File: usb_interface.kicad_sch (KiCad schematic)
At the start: 56 parts, among them J7 GCT USB4105-GF-A-120, J8 PD_I2C DEBUG, Q1 CSD25480F3, Q2 CSD15380F3, Q3 CSD25480F3, Q4 CSD15380F3, U3 TVS2200DRV, U4 TPD8S300/A, U5 TI TPS25751DREFR, U6 CAT24C256

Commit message: oops add this
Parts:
- removed C35: 10uF, Capacitor_SMD:C_1206_3216Metric, symbol Device:C_Small
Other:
- note added: "7 x 10uF"
- note removed: "8 x 10uF"
- moved on the sheet: C26, C27, C29, C30, C32, C34

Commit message: assign lcsc part numbers
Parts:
- C26, C29, C30, C32, C34: LCSC Part C14860 -> C33546013
- C27, C28: LCSC Part C49326770 -> C33546013
- R35, R38: LCSC Part C2902636 -> C54951138
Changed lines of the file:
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@@
 			)
 		)
-		(property "LCSC Part" "C14860"
+		(property "LCSC Part" "C33546013"
 			(at 114.3 66.04 0)
 			(hide yes)
@@
 			)
 		)
-		(property "LCSC Part" "C14860"
+		(property "LCSC Part" "C33546013"
 			(at 118.11 66.04 0)
 			(hide yes)
@@
 			)
 		)
-		(property "LCSC Part" "C49326770"
+		(property "LCSC Part" "C33546013"
 			(at 110.49 66.04 0)
 			(hide yes)
@@
 			)
 		)
-		(property "LCSC Part" "C2902636"
+		(property "LCSC Part" "C54951138"
 			(at 232.41 74.93 0)
 			(hide yes)
@@
 			)
 		)
-		(property "LCSC Part" "C49326770"
+		(property "LCSC Part" "C33546013"
 			(at 106.68 66.04 0)
 			(hide yes)
@@
 			)
 		)
-		(property "LCSC Part" "C14860"
+		(property "LCSC Part" "C33546013"
 			(at 102.87 66.04 0)
 			(hide yes)
@@
 			)
 		)
-		(property "LCSC Part" "C2902636"
+		(property "LCSC Part" "C54951138"
 			(at 181.61 60.96 0)
 			(hide yes)
@@
 			)
 		)
-		(property "LCSC Part" "C14860"
+		(property "LCSC Part" "C33546013"
 			(at 125.73 66.04 0)
 			(hide yes)
@@
 			)
 		)
-		(property "LCSC Part" "C14860"
+		(property "LCSC Part" "C33546013"
 			(at 121.92 66.04 0)
 			(hide yes)

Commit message: new part numbers for out of stock components
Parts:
- Q1, Q3: LCSC Part C2869359 -> C2872850
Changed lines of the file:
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@@
 			)
 		)
-		(property "LCSC Part" "C2869359"
+		(property "LCSC Part" "C2872850"
 			(at 68.58 146.05 0)
 			(hide yes)
@@
 			)
 		)
-		(property "LCSC Part" "C2869359"
+		(property "LCSC Part" "C2872850"
 			(at 45.72 146.05 0)
 			(hide yes)

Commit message: backup before switching to kicad-nightly
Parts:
- J7: value GCT USB4105-GF-A-120 -> GCT USB4105-GF-A-060
- Q1, Q3: value CSD25480F3 -> CSD25481F4
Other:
- moved on the sheet: Q1, Q3
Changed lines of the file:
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@@
 	(wire
 		(pts
-			(xy 48.26 151.13) (xy 48.26 153.67)
+			(xy 48.26 152.4) (xy 48.26 153.67)
 		)
 		(stroke
@@
 	(wire
 		(pts
+			(xy 71.12 142.24) (xy 71.12 140.97)
+		)
+		(stroke
+			(width 0)
+			(type default)
+		)
+	)
+	(wire
+		(pts
 			(xy 181.61 114.3) (xy 181.61 116.84)
 		)
@@
 	(wire
 		(pts
+			(xy 48.26 142.24) (xy 48.26 140.97)
+		)
+		(stroke
+			(width 0)
+			(type default)
+		)
+	)
+	(wire
+		(pts
 			(xy 35.56 27.94) (xy 38.1 27.94)
 		)
@@
 	(wire
 		(pts
-			(xy 71.12 151.13) (xy 71.12 153.67)
+			(xy 71.12 152.4) (xy 71.12 153.67)
 		)
 		(stroke
@@
 	)
 	(label "GPIO2"
-		(at 63.5 146.05 180)
+		(at 63.5 147.32 180)
 		(effects
 			(font
@@
 	)
 	(label "GPIO2"
-		(at 40.64 146.05 180)
+		(at 40.64 147.32 180)
 		(effects
 			(font
@@
 	(symbol
 		(lib_id "Transistor_FET:CSD25480F3")
-		(at 68.58 146.05 0)
+		(at 68.58 147.32 0)
 		(mirror x)
 		(unit 1)
@@
 		(dnp no)
 		(property "Reference" "Q3"
-			(at 65.532 142.494 0)
+			(at 65.532 143.764 0)
 			(show_name no)
 			(do_not_autoplace no)
@@
 			)
 		)
-		(property "Value" "CSD25480F3"
-			(at 71.882 149.352 0)
+		(property "Value" "CSD25481F4"
+			(at 71.882 150.622 0)
 			(show_name no)
 			(do_not_autoplace no)
@@
 		)
 		(property "Footprint" "Package_DFN_QFN:Texas_PicoStar_DFN-3_0.69x0.60mm"
-			(at 98.933 141.351 0)
+			(at 98.933 142.621 0)
 			(hide yes)
 			(show_name no)
@@
 		)
 		(property "Datasheet" "https://www.ti.com/lit/ds/symlink/csd25480f3.pdf"
-			(at 99.695 143.637 0)
+			(at 99.695 144.907 0)
 			(hide yes)
 			(show_name no)
@@
 		)
 		(property "Description" "-1.7A Id, -20V Vds, P-Channel MOSFET, 159mOhm Ron,max @ 4.5Vgs, 0.70nC Qg,typ @ 4.5Vgs, PicoStar 0.73x0.64mm max, 0.69x0.60mm nom"
-			(at 68.58 146.05 0)
+			(at 68.58 147.32 0)
 			(hide yes)
 			(show_name no)
@@
 		)
 		(property "LCSC Part" "C2872850"
-			(at 68.58 146.05 0)
+			(at 68.58 147.32 0)
 			(hide yes)
 			(show_name no)
@@
 		)
 		(property "Voltage Rating" ""
-			(at 68.58 146.05 0)
+			(at 68.58 147.32 0)
 			(hide yes)
 			(show_name no)
@@
 		)
 		(property "Tolerance" ""
-			(at 68.58 146.05 0)
+			(at 68.58 147.32 0)
 			(hide yes)
 			(show_name no)
@@
 		)
 		(property "Capacitor Rating" ""
-			(at 68.58 146.05 0)
+			(at 68.58 147.32 0)
 			(hide yes)
 			(show_name no)
@@
 			)
 		)
-		(property "Value" "GCT USB4105-GF-A-120"
+		(property "Value" "GCT USB4105-GF-A-060"
 			(at 77.47 68.58 0)
 			(show_name no)
@@
 			)
 		)
+		(property "Capacitor Rating" ""
+			(at 77.47 88.9 0)
+			(hide yes)
+			(show_name no)
+			(do_not_autoplace no)
+			(effects
+				(font
+					(size 1.27 1.27)
+				)
+			)
+		)
 		(pin "B6"
 		)
@@
 	(symbol
 		(lib_id "Transistor_FET:CSD25480F3")
-		(at 45.72 146.05 0)
+		(at 45.72 147.32 0)
 		(mirror x)
 		(unit 1)
@@
 		(dnp no)
 		(property "Reference" "Q1"
-			(at 42.418 142.494 0)
+			(at 42.418 143.764 0)
 			(show_name no)
 			(do_not_autoplace no)
@@
 			)
 		)
-		(property "Value" "CSD25480F3"
-			(at 49.53 149.352 0)
+		(property "Value" "CSD25481F4"
+			(at 49.53 150.622 0)
 			(show_name no)
 			(do_not_autoplace no)
@@
 		)
 		(property "Footprint" "Package_DFN_QFN:Texas_PicoStar_DFN-3_0.69x0.60mm"
-			(at 76.073 141.351 0)
+			(at 76.073 142.621 0)
 			(hide yes)
 			(show_name no)
@@
 		)
 		(property "Datasheet" "https://www.ti.com/lit/ds/symlink/csd25480f3.pdf"
-			(at 76.835 143.637 0)
+			(at 76.835 144.907 0)
 			(hide yes)
 			(show_name no)
@@
 		)
 		(property "Description" "-1.7A Id, -20V Vds, P-Channel MOSFET, 159mOhm Ron,max @ 4.5Vgs, 0.70nC Qg,typ @ 4.5Vgs, PicoStar 0.73x0.64mm max, 0.69x0.60mm nom"
-			(at 45.72 146.05 0)
+			(at 45.72 147.32 0)
 			(hide yes)
 			(show_name no)
@@
 		)
 		(property "LCSC Part" "C2872850"
-			(at 45.72 146.05 0)
+			(at 45.72 147.32 0)
 			(hide yes)
 			(show_name no)
@@
 		)
 		(property "Voltage Rating" ""
-			(at 45.72 146.05 0)
+			(at 45.72 147.32 0)
 			(hide yes)
 			(show_name no)
@@
 		)
 		(property "Tolerance" ""
-			(at 45.72 146.05 0)
+			(at 45.72 147.32 0)
 			(hide yes)
 			(show_name no)
@@
 		)
 		(property "Capacitor Rating" ""
-			(at 45.72 146.05 0)
+			(at 45.72 147.32 0)
 			(hide yes)
 			(show_name no)

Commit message: lots of fixes!
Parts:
- removed U6: CAT24C256, Package_DFN_QFN:DFN-8-1EP_2x3mm_P0.5mm_EP0.61x2.2mm, symbol Memory_EEPROM:CAT24C256
- added U21: M24512-DFMC6TG, Package_DFN_QFN:DFN-8-1EP_3x2mm_P0.5mm_EP1.36x1.46mm, symbol easyeda2kicad:M24512-DFMC6TG
- C33, C36: LCSC Part C190579 -> C53426851
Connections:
- net GND: now also U21.4 (GND), U21.9 (EP)
- net I2C_PMIC_SCL: now also U21.6 (SCL)
- net I2C_PMIC_SDA: now also U21.5 (SDA)
- net PD_LDO_3V3: now also U21.8 (VCC)
- net WC: now also U21.7 (WC)
- net at RN1.5 (R4.2): now also U21.3 (E2)
- net at RN1.6 (R3.2): now also U21.2 (E1)
- net at RN1.7 (R2.2): now also U21.1 (E0)
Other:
- note added: "EEPROM 512Kb"
- note removed: "EEPROM 256Kb"
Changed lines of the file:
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@@
 (kicad_sch
-	(version 20260306)
+	(version 20260830)
 	(generator "eeschema")
-	(generator_version "10.0")
+	(generator_version "10.99")
 	(paper "A4")
 	(title_block
@@
 		)
 	)
-	(text "EEPROM 256Kb"
+	(text "EEPROM 512Kb"
 		(exclude_from_sim no)
 		(at 267.716 81.534 0)
@@
 	)
 	(junction
+		(at 241.3 104.14)
+		(diameter 0)
+		(color 0 0 0 0)
+	)
+	(junction
 		(at 71.12 140.97)
 		(diameter 0)
@@
 	(wire
 		(pts
+			(xy 241.3 104.14) (xy 243.84 104.14)
+		)
+		(stroke
+			(width 0)
+			(type default)
+		)
+	)
+	(wire
+		(pts
 			(xy 243.84 105.41) (xy 243.84 104.14)
 		)
@@
 	(wire
 		(pts
+			(xy 241.3 100.33) (xy 241.3 104.14)
+		)
+		(stroke
+			(width 0)
+			(type default)
+		)
+	)
+	(wire
+		(pts
 			(xy 118.11 63.5) (xy 118.11 62.23)
 		)
@@
 	(wire
 		(pts
-			(xy 229.87 104.14) (xy 243.84 104.14)
+			(xy 229.87 104.14) (xy 241.3 104.14)
 		)
 		(stroke
@@
 	)
 	(symbol
-		(lib_id "Memory_EEPROM:CAT24C256")
-		(at 243.84 90.17 0)
-		(unit 1)
-		(body_style 1)
-		(exclude_from_sim no)
-		(in_bom yes)
-		(on_board yes)
-		(in_pos_files yes)
-		(dnp no)
-		(property "Reference" "U6"
-			(at 234.442 81.026 0)
-			(show_name no)
-			(do_not_autoplace no)
-			(effects
-				(font
-					(size 1.27 1.27)
-				)
-				(justify left)
-			)
-		)
-		(property "Value" "CAT24C256"
-			(at 245.364 99.822 0)
-			(show_name no)
-			(do_not_autoplace no)
-			(effects
-				(font
-					(size 1.27 1.27)
-				)
-				(justify left)
-			)
-		)
-		(property "Footprint" "Package_DFN_QFN:DFN-8-1EP_2x3mm_P0.5mm_EP0.61x2.2mm"
-			(at 243.84 90.17 0)
-			(hide yes)
-			(show_name no)
-			(do_not_autoplace no)
-			(effects
-				(font
-					(size 1.27 1.27)
-				)
-			)
-		)
-		(property "Datasheet" "https://www.onsemi.cn/PowerSolutions/document/CAT24C256-D.PDF"
-			(at 241.808 108.204 0)
-			(hide yes)
-			(show_name no)
-			(do_not_autoplace no)
-			(effects
-				(font
-					(size 1.27 1.27)
-				)
-			)
-		)
-		(property "Description" "256 kb CMOS Serial EEPROM, DIP-8/SOIC-8/TSSOP-8/DFN-8"
-			(at 241.808 108.204 0)
-			(hide yes)
-			(show_name no)
-			(do_not_autoplace no)
-			(effects
-				(font
-					(size 1.27 1.27)
-				)
-			)
-		)
-		(property "LCSC Part" "C233771"
-			(at 243.84 90.17 0)
-			(hide yes)
-			(show_name no)
-			(do_not_autoplace no)
-			(effects
-				(font
-					(size 1.27 1.27)
-				)
-			)
-		)
-		(property "Voltage Rating" ""
-			(at 243.84 90.17 0)
-			(hide yes)
-			(show_name no)
-			(do_not_autoplace no)
-			(effects
-				(font
-					(size 1.27 1.27)
-				)
-			)
-		)
-		(property "Tolerance" ""
-			(at 243.84 90.17 0)
-			(hide yes)
-			(show_name no)
-			(do_not_autoplace no)
-			(effects
-				(font
-					(size 1.27 1.27)
-				)
-			)
-		)
-		(property "Capacitor Rating" ""
-			(at 243.84 90.17 0)
-			(hide yes)
-			(show_name no)
-			(do_not_autoplace no)
-			(effects
-				(font
-					(size 1.27 1.27)
-				)
-			)
-		)
-		(pin "7"
-		)
-		(pin "6"
-		)
-		(pin "5"
-		)
-		(pin "4"
-		)
-		(pin "3"
-		)
-		(pin "2"
-		)
-		(pin "1"
-		)
-		(pin "8"
-		)
-		(instances
-			(project "parsnip"
-				(path "/a9f1fdad-fb49-4185-a4ff-ad8f47273e4d"
-					(reference "U6")
-					(unit 1)
-				)
-			)
-		)
-	)
-	(symbol
 		(lib_id "Device:C_Small")
 		(at 54.61 88.9 0)
@@
 		(dnp no)
 		(property "Reference" "R36"
-			(at 183.642 55.88 0)
+			(at 184.15 53.848 0)
 			(show_name no)
 			(do_not_autoplace no)
@@
 		)
 		(property "Value" "2.2k"
-			(at 183.388 64.516 0)
+			(at 183.642 55.88 0)
 			(show_name no)
 			(do_not_autoplace no)
@@
 			)
 		)
-		(property "LCSC Part" "C190579"
+		(property "LCSC Part" "C53426851"
 			(at 129.54 85.09 0)
 			(hide yes)
@@
 			)
 		)
+		(property "MPN" ""
+			(at 129.54 85.09 0)
+			(hide yes)
+			(show_name no)
+			(do_not_autoplace no)
+			(effects
+				(font
+					(size 1.27 1.27)
+				)
+			)
+		)
 		(pin "1"
 		)
@@
 	)
 	(symbol
+		(lib_id "easyeda2kicad:M24512-DFMC6TG")
+		(at 242.57 86.36 0)
+		(unit 1)
+		(body_style 1)
+		(exclude_from_sim no)
+		(in_bom yes)
+		(on_board yes)
+		(in_pos_files yes)
+		(dnp no)
+		(property "Reference" "U21"
+			(at 236.474 81.28 0)
+			(show_name no)
+			(do_not_autoplace no)
+			(effects
+				(font
+					(size 1.27 1.27)
+				)
+			)
+		)
+		(property "Value" "M24512-DFMC6TG"
+			(at 254.254 99.822 0)
+			(show_name no)
+			(do_not_autoplace no)
+			(effects
+				(font
+					(size 1.27 1.27)
+				)
+			)
+		)
+		(property "Footprint" "Package_DFN_QFN:DFN-8-1EP_3x2mm_P0.5mm_EP1.36x1.46mm"
+			(at 243.84 109.728 0)
+			(hide yes)
+			(show_name no)
+			(do_not_autoplace no)
+			(effects
+				(font
+					(size 1.27 1.27)
+				)
+			)
+		)
+		(property "Datasheet" "https://lcsc.com/product-detail/Others_STMicroelectronics_M24512-DFMC6TG_STMicroelectronics-M24512-DFMC6TG_C222237.html"
+			(at 243.84 112.268 0)
+			(hide yes)
+			(show_name no)
+			(do_not_autoplace no)
+			(effects
+				(font
+					(size 1.27 1.27)
+				)
+			)
+		)
+		(property "Description" ""
+			(at 242.57 86.36 0)
+			(hide yes)
+			(show_name no)
+			(do_not_autoplace no)
+			(effects
+				(font
+					(size 1.27 1.27)
+				)
+			)
+		)
+		(property "Manufacturer" "ST(意法半导体)"
+			(at 243.84 114.808 0)
+			(hide yes)
+			(show_name no)
+			(do_not_autoplace no)
+			(effects
+				(font
+					(size 1.27 1.27)
+				)
+			)
+		)
+		(property "MPN" "M24512-DFMC6TG"
+			(at 243.84 117.348 0)
+			(hide yes)
+			(show_name no)
+			(do_not_autoplace no)
+			(effects
+				(font
+					(size 1.27 1.27)
+				)
+			)
+		)
+		(property "LCSC Part" "C222237"
+			(at 243.84 119.888 0)
+			(hide yes)
+			(show_name no)
+			(do_not_autoplace no)
+			(effects
+				(font
+					(size 1.27 1.27)
+				)
+			)
+		)
+		(property "Voltage Rating" ""
+			(at 242.57 86.36 0)
+			(hide yes)
+			(show_name no)
+			(do_not_autoplace no)
+			(effects
+				(font
+					(size 1.27 1.27)
+				)
+			)
+		)
+		(property "Tolerance" ""
+			(at 242.57 86.36 0)
+			(hide yes)
+			(show_name no)
+			(do_not_autoplace no)
+			(effects
+				(font
+					(size 1.27 1.27)
+				)
+			)
+		)
+		(pin "1"
+		)
+		(pin "2"
+		)
+		(pin "3"
+		)
+		(pin "4"
+		)
+		(pin "5"
+		)
+		(pin "6"
+		)
+		(pin "7"
+		)
+		(pin "8"
+		)
+		(pin "9"
+		)
+		(instances
+			(project "parsnip"
+				(path "/a9f1fdad-fb49-4185-a4ff-ad8f47273e4d"
+					(reference "U21")
+					(unit 1)
+				)
+			)
+		)
+	)
+	(symbol
 		(lib_id "Device:C_Small")
 		(at 102.87 66.04 0)
@@
 			)
 		)
-		(property "LCSC Part" "C190579"
+		(property "LCSC Part" "C53426851"
 			(at 121.92 85.09 0)
 			(hide yes)
@@
 			(at 121.92 85.09 0)
 			(hide yes)
+			(show_name no)
+			(do_not_autoplace no)
+			(effects
+				(font
+					(size 1.27 1.27)
+				)
+			)
+		)
+		(property "MPN" ""
+			(at 121.92 85.09 0)
+			(hide yes)

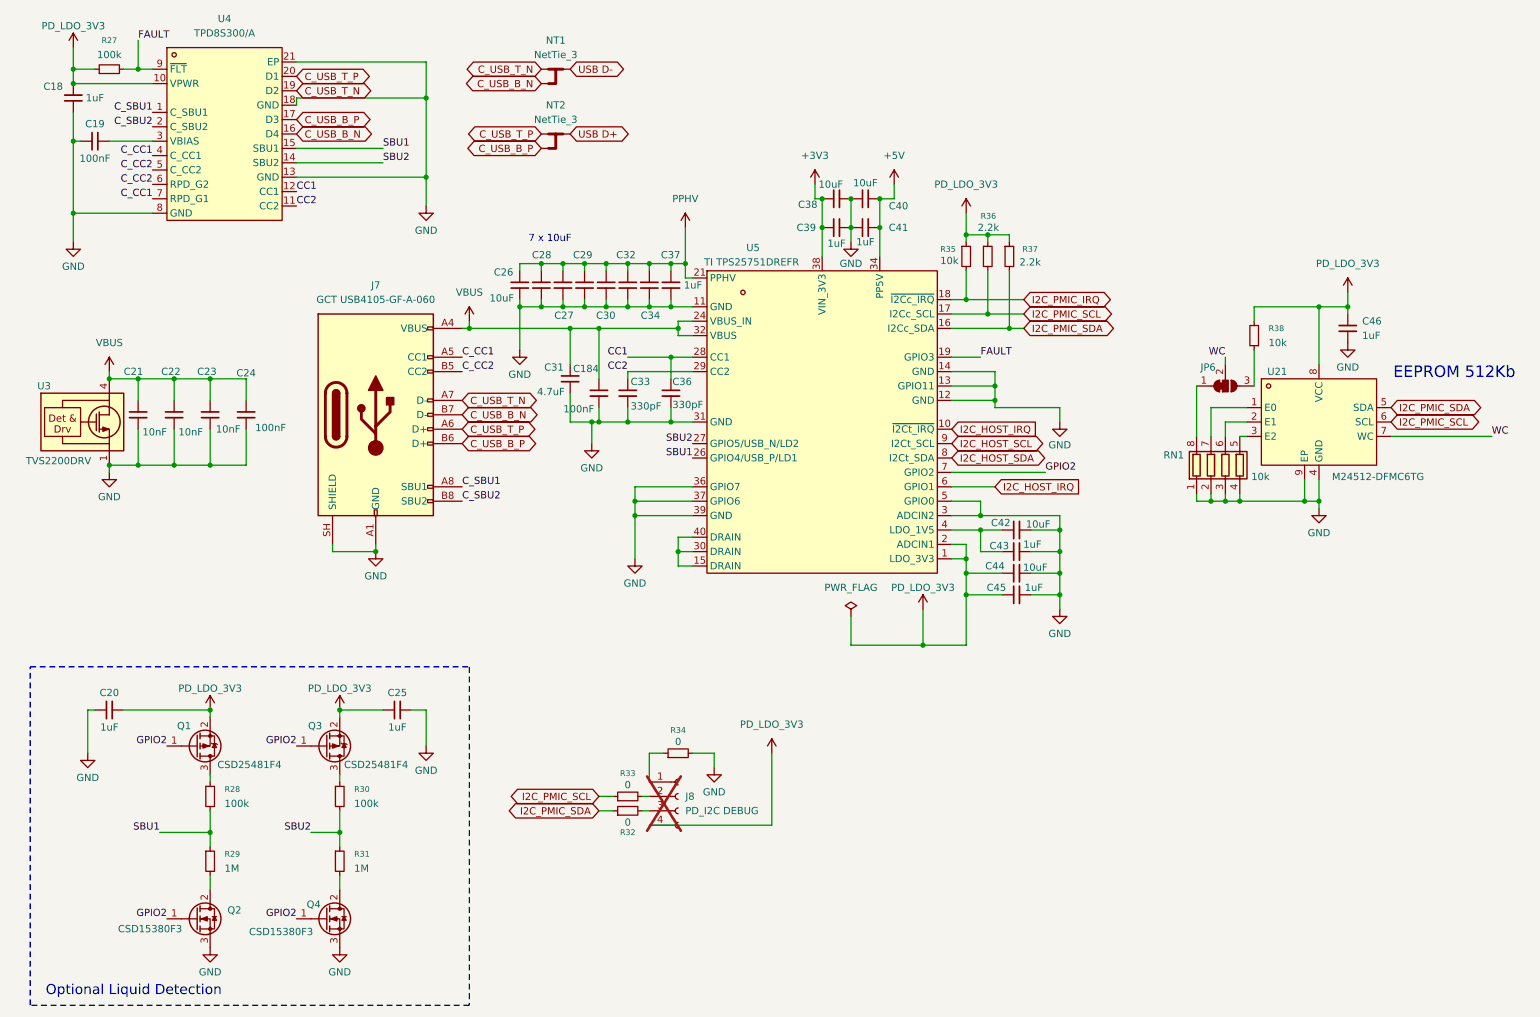
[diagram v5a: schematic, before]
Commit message: fix bug with using GDS instead of GSD FET
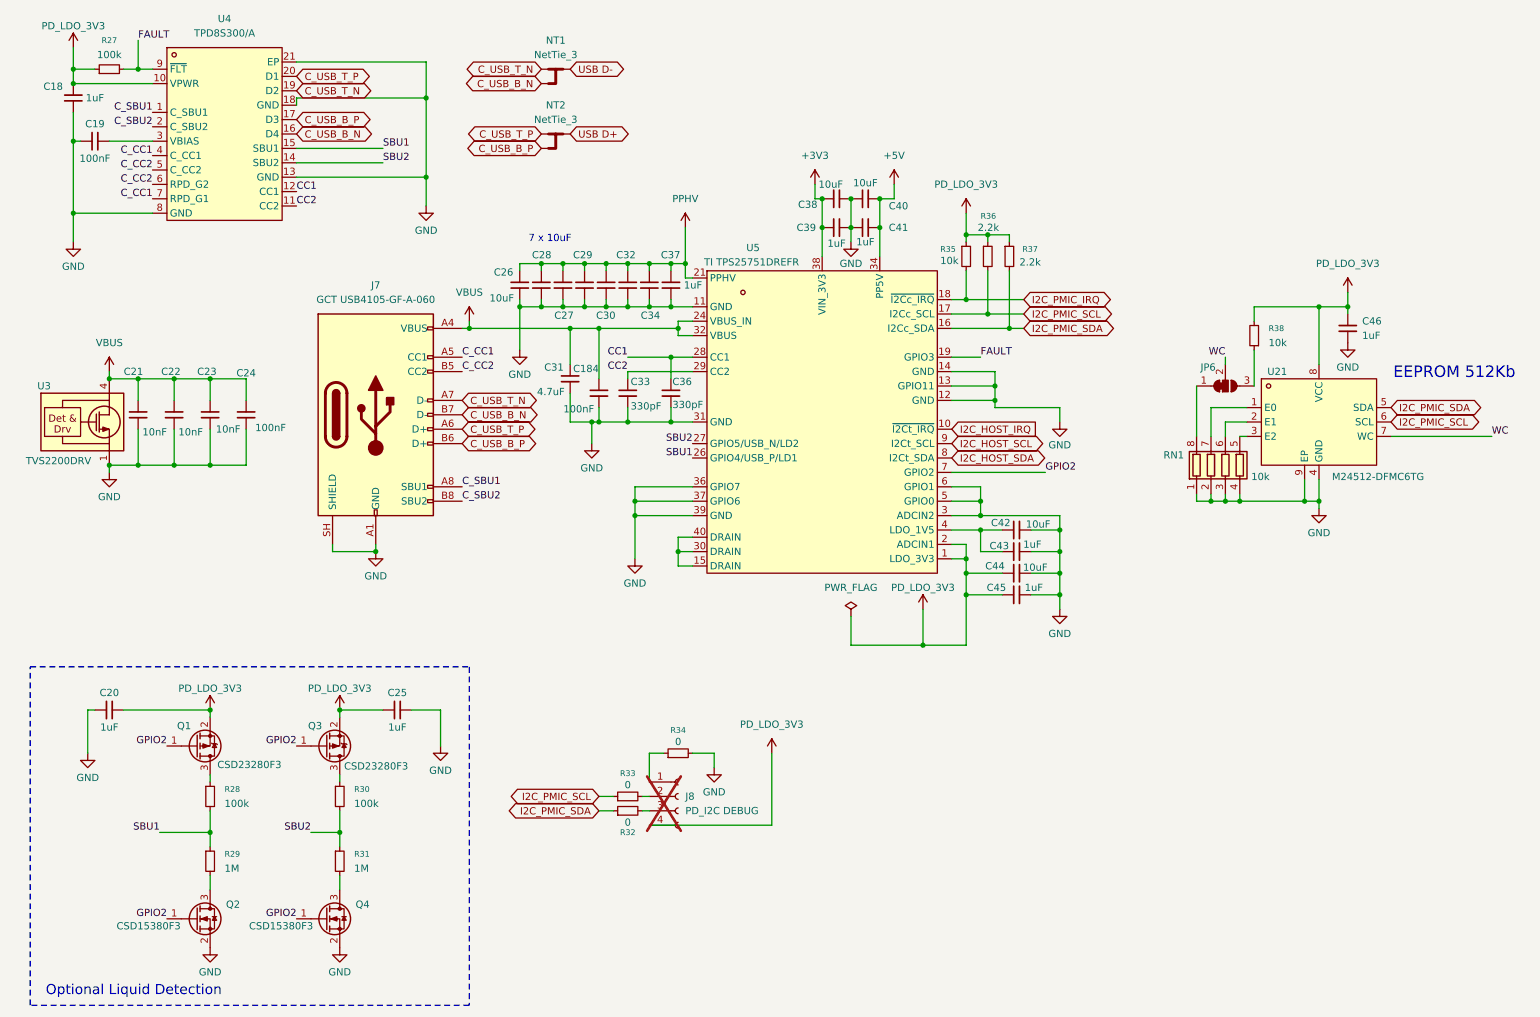
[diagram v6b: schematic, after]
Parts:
- removed Q2, Q4: CSD15380F3, Package_DFN_QFN:Texas_PicoStar_DFN-3_0.69x0.60mm, symbol Transistor_FET:Q_NMOS_GDS
- added Q2, Q4: CSD15380F3, Package_DFN_QFN:Texas_PicoStar_DFN-3_0.69x0.60mm, symbol Transistor_FET:Q_NMOS_GSD
- Q1, Q3: value CSD25481F4 -> CSD23280F3; LCSC Part C2872850 -> C139374
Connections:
- net GND: now also U5.6 (GPIO1), Q2.2 (S), Q4.2 (S)
- net GPIO2: now also Q2.1 (G), Q4.1 (G)
- net I2C_HOST_IRQ: no longer U5.6 (GPIO1)
- net at R29.2: now also Q2.3 (D)
- net at R31.2: now also Q4.3 (D)
